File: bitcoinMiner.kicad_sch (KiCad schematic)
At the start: 14 parts, among them U1 BM1370_mode1, U2 25MHz, U3 MCP1824T-1202E/OT, U4 MCP1824T-0802E

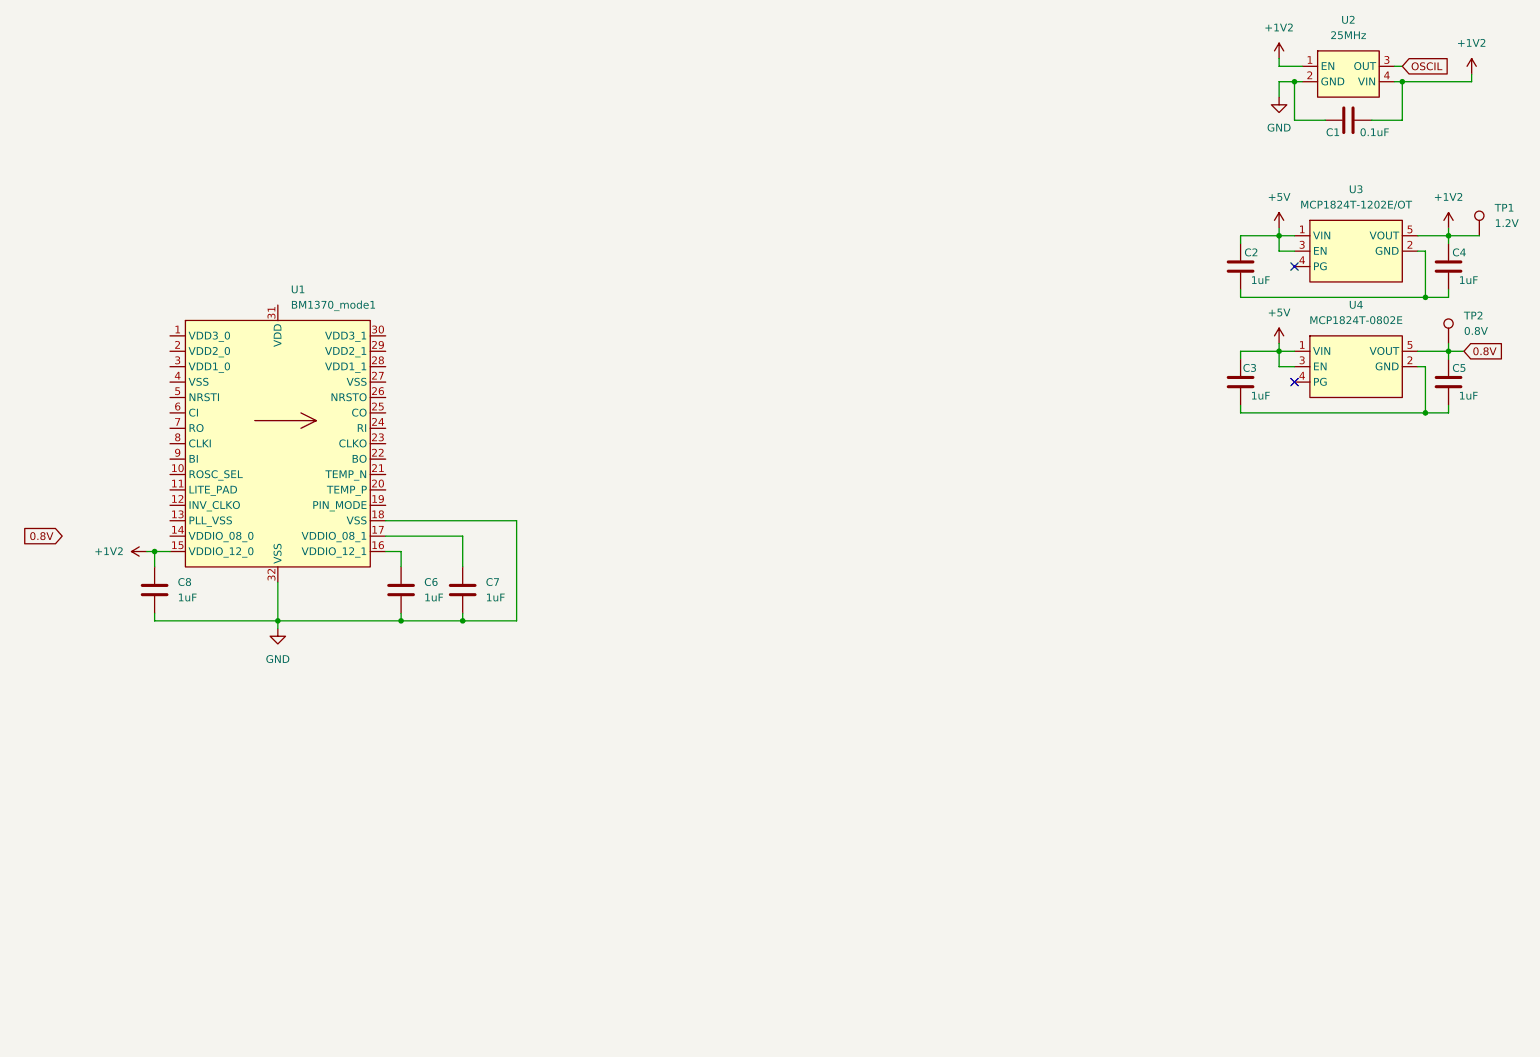
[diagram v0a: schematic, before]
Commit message: finish copying schematic from bitaxe
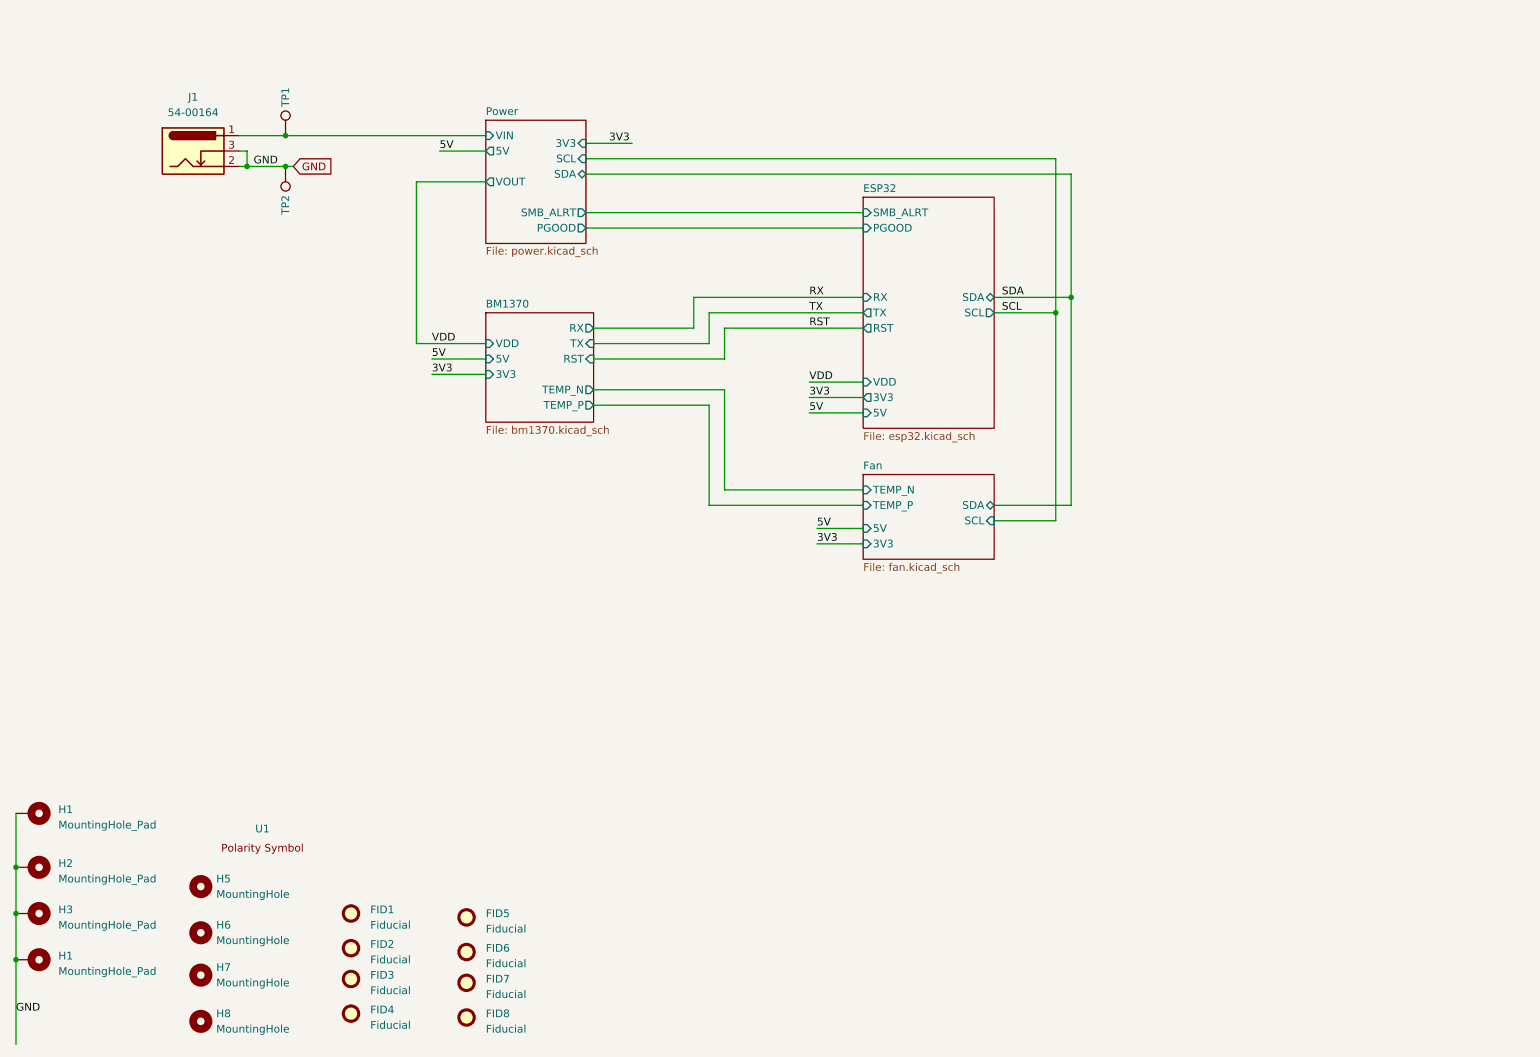
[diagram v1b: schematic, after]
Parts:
- removed C1: 0.1uF, symbol Device:C
- removed C2, C3, C4, C5, C6, C7, C8: 1uF, symbol Device:C
- removed U1: BM1370_mode1, bitaxe:BM1370, symbol bitaxe:BM1370_mode1
- removed U2: 25MHz, symbol bitaxe:oscillator
- removed U3: MCP1824T-1202E/OT, Package_TO_SOT_SMD:SOT-23-5, symbol bitaxe:MCP1824
- removed U4: MCP1824T-0802E, Package_TO_SOT_SMD:SOT-23-5, symbol bitaxe:MCP1824
- added FID1, FID2, FID3, FID4, FID5, FID6, FID7, FID8: Fiducial, Fiducial:Fiducial_1mm_Mask2mm, symbol Mechanical:Fiducial
- added H1 (x2), H2, H3: MountingHole_Pad, MountingHole:MountingHole_3mm_Pad_Via, symbol Mechanical:MountingHole_Pad
- added H5, H6, H7, H8: MountingHole, MountingHole:MountingHole_3.5mm, symbol Mechanical:MountingHole
- added J1: 54-00164, bitaxe:TENSILITY_54-00164, symbol Connector:Barrel_Jack_Switch
- added U1: ~, bitaxe:polarity, symbol bitaxe:polarity
- TP1: value 1.2V -> TestPoint; now left out of the parts list
- TP2: value 0.8V -> TestPoint; now left out of the parts list
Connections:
- net 0.8V is gone; now on net GND: TP2.1
- net GND: now also H1.1, H1.1, H2.1, H3.1, J1.2, J1.3
- net +1V2 renamed Power/VIN
- net Power/VIN: now also J1.1
- no-connect marks 2 -> 0
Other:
- added sheet BM1370 (bm1370.kicad_sch)
- added sheet ESP32 (esp32.kicad_sch)
- added sheet Fan (fan.kicad_sch)
- added sheet Power (power.kicad_sch)
